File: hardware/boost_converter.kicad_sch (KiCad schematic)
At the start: 12 parts, among them J2 Conn_01x02_Pin, U3 SparkFun_LiPower, U4 TPS61200DRC

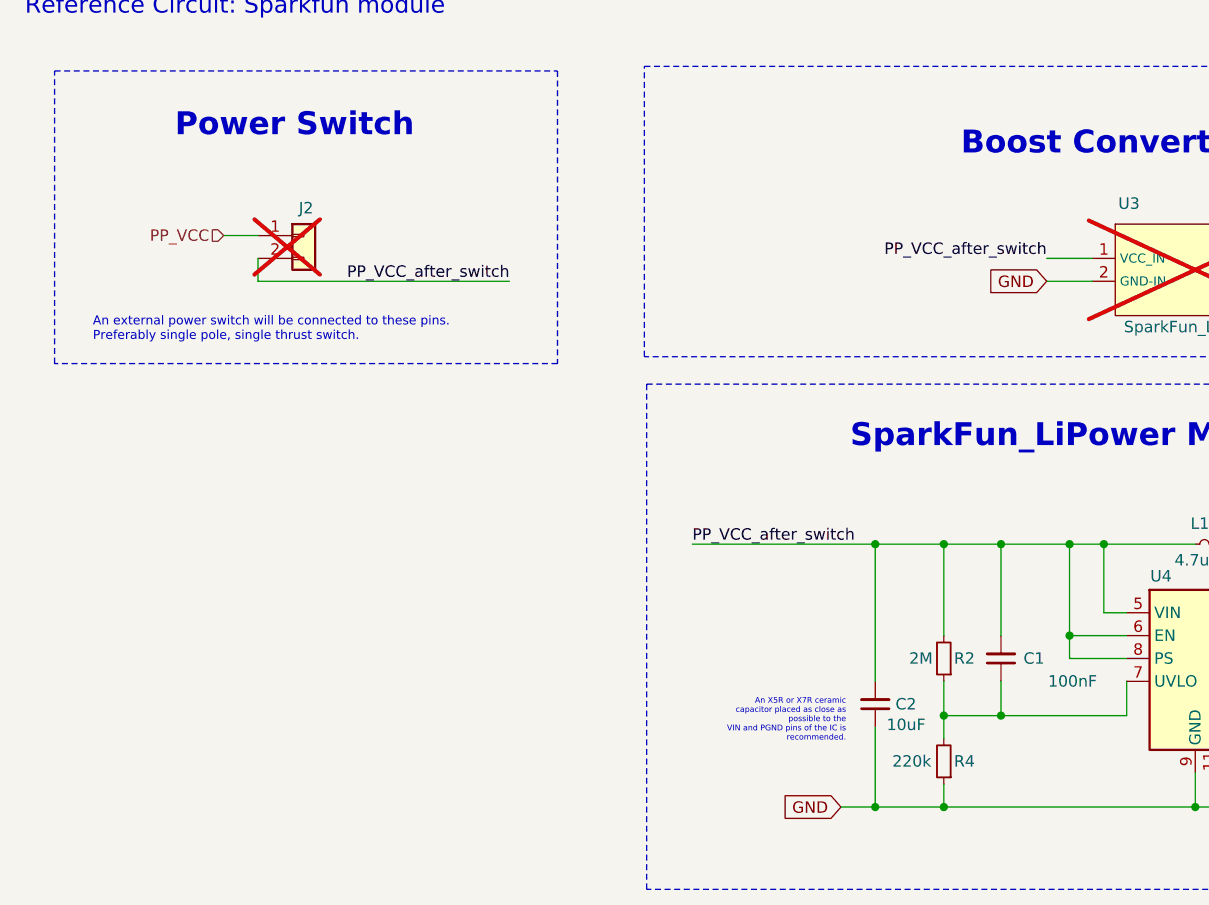
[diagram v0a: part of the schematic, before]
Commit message: Added Tx resistor, voltage devider for battery voltage mesurement.
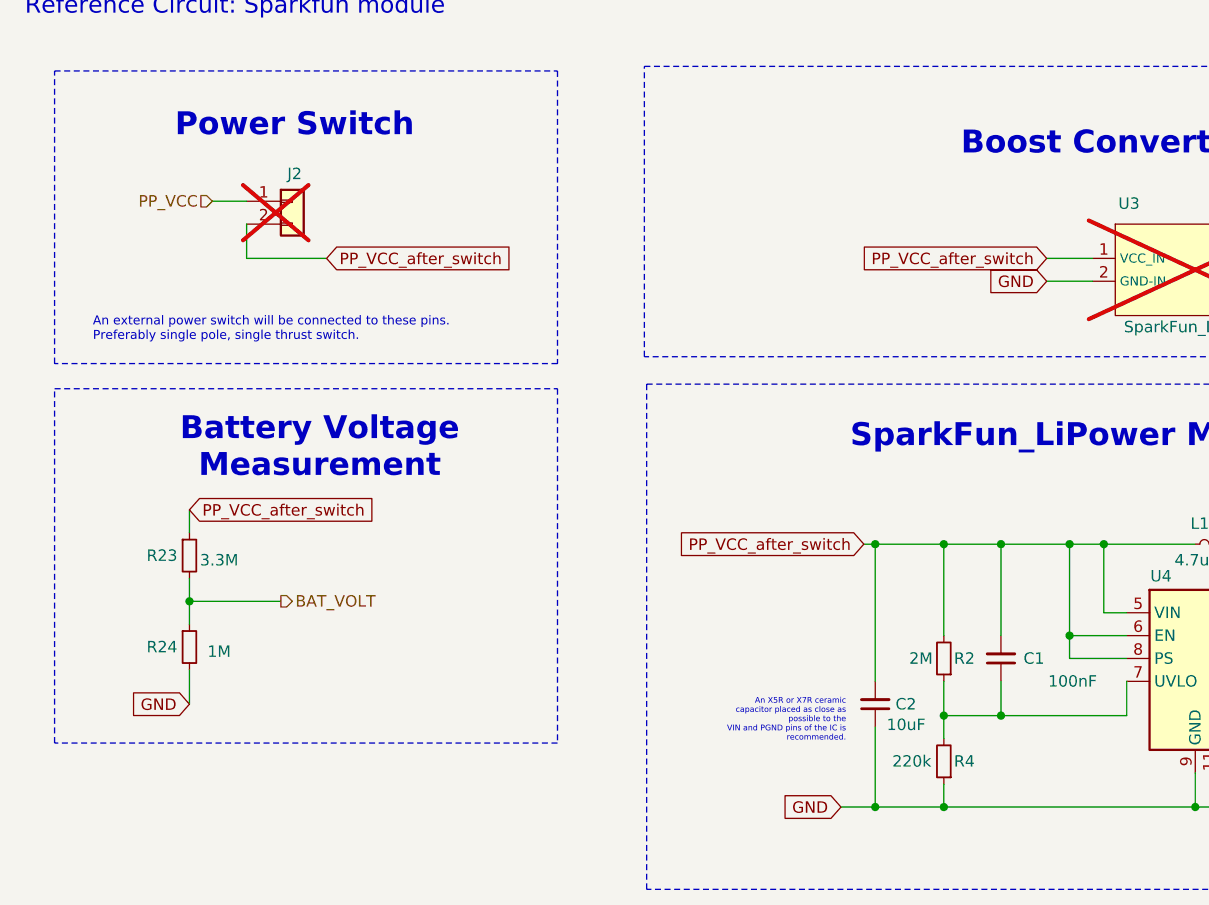
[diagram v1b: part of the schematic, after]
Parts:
- added R23: 3.3M, Resistor_SMD:R_0805_2012Metric_Pad1.20x1.40mm_HandSolder, symbol Device:R_Small
- added R24: 1M, Resistor_SMD:R_0805_2012Metric_Pad1.20x1.40mm_HandSolder, symbol Device:R_Small
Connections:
- net GND: now also R24.2
- net PP_VCC_after_switch: now also R23.1
- new net BAT_VOLT: R23.2, R24.1
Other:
- note added: "Battery Voltage Measurement"
- moved on the sheet: J2
